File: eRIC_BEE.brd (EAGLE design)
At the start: 25.2 x 34 mm, 40 parts

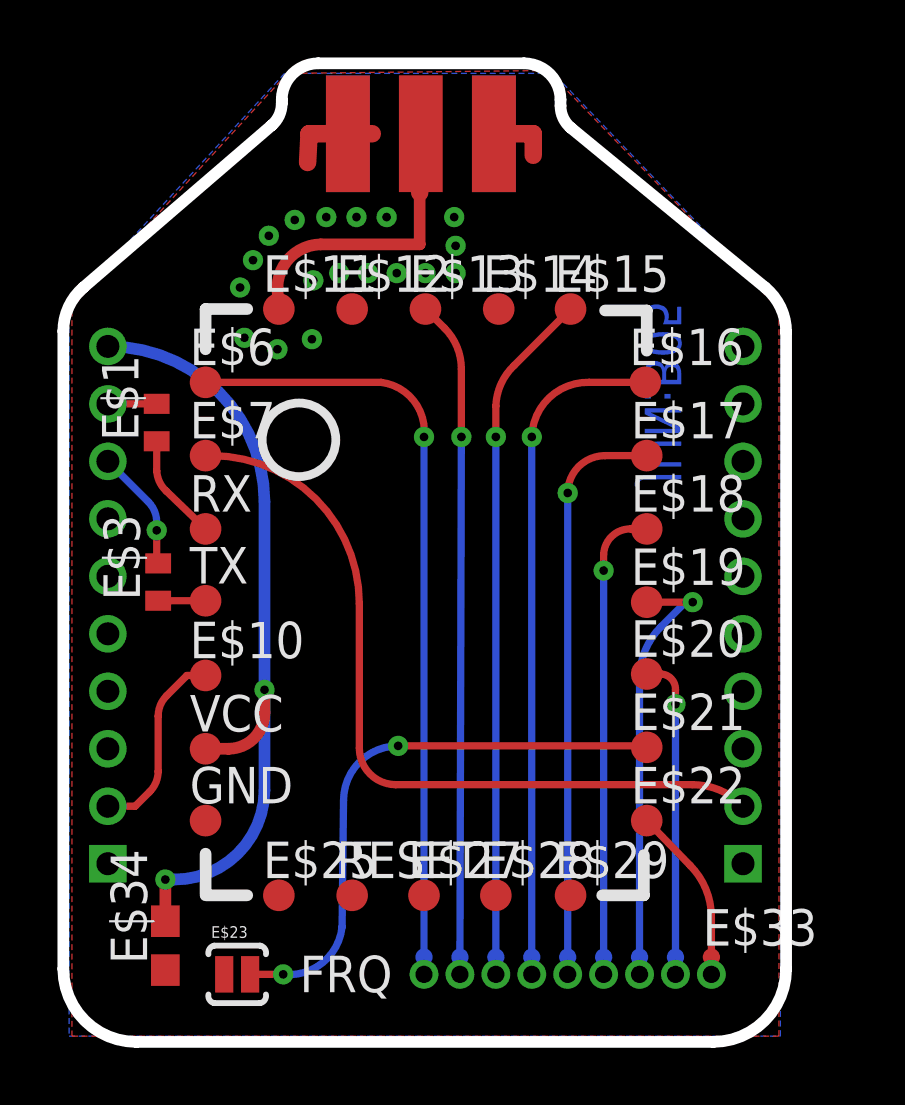
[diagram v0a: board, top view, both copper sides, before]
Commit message: board outline, widen pin spacing, move SMA connector forward
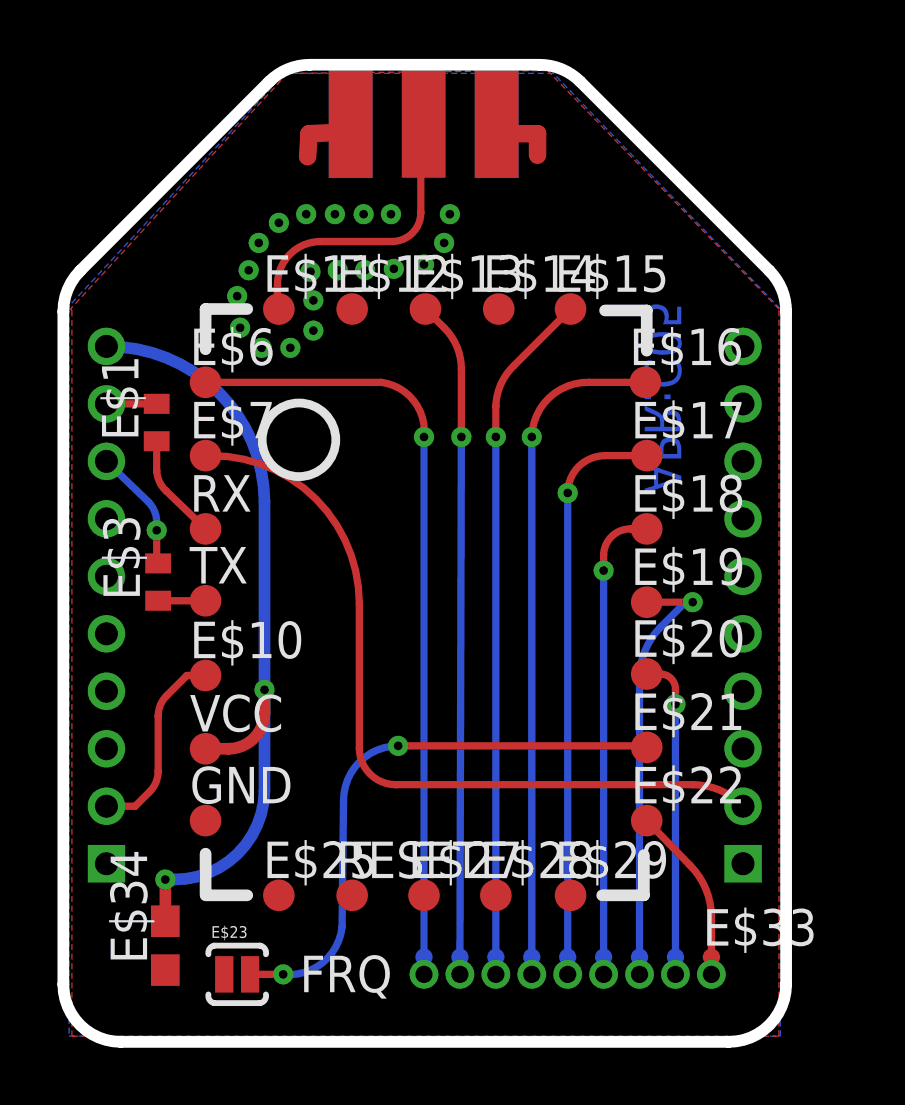
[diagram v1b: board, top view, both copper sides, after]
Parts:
- moved E$44 0.51 mm to (17.9, 47.5)
- moved E$24 0.05 mm to (9.45, 21.6)
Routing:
- net GND: track 5.25 -> 4.10 mm, vias 18 -> 20
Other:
- outline, holes or cut-outs redrawn
- board text added: "APR:C05"
- board text removed: "JUN:B05"
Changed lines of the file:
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@@
 <wire x1="28.25" y1="40.8" x2="26.8" y2="40.8" width="0.4064" layer="121"/>
 <wire x1="28.25" y1="39.4" x2="28.25" y2="40.8" width="0.4064" layer="121"/>
-<wire x1="15.20244375" y1="47.243825" x2="8.6451125" y2="41.598440625" width="0.4064" layer="20"/>
-<wire x1="8.6451125" y1="41.598440625" x2="7.95" y2="40.082765625" width="0.4064" layer="20" curve="49.273877"/>
-<wire x1="7.95" y1="40.082765625" x2="7.95" y2="17.89" width="0.4064" layer="20"/>
-<wire x1="7.95" y1="17.89" x2="10.49" y2="15.35" width="0.4064" layer="20" curve="90"/>
-<wire x1="10.49" y1="15.35" x2="30.56" y2="15.35" width="0.4064" layer="20"/>
-<wire x1="30.56" y1="15.35" x2="33.1" y2="17.89" width="0.4064" layer="20" curve="90"/>
-<wire x1="33.1" y1="17.89" x2="33.1" y2="40.054784375" width="0.4064" layer="20"/>
-<wire x1="33.1" y1="40.054784375" x2="32.3696875" y2="41.600065625" width="0.4064" layer="20" curve="50.591606"/>
-<wire x1="32.3696875" y1="41.600065625" x2="25.61515625" y2="47.149965625" width="0.4064" layer="20"/>
-<wire x1="25.61515625" y1="47.149965625" x2="25.25" y2="47.92260625" width="0.4064" layer="20" curve="-50.591606"/>
-<wire x1="25.25" y1="47.92260625" x2="25.25" y2="48.13" width="0.4064" layer="20"/>
-<wire x1="25.25" y1="48.13" x2="23.98" y2="49.4" width="0.4064" layer="20" curve="90"/>
-<wire x1="23.98" y1="49.4" x2="16.82" y2="49.4" width="0.4064" layer="20"/>
-<wire x1="16.82" y1="49.4" x2="15.55" y2="48.13" width="0.4064" layer="20" curve="90"/>
-<wire x1="15.55" y1="48.13" x2="15.55" y2="48.0016625" width="0.4064" layer="20"/>
-<wire x1="15.55" y1="48.0016625" x2="15.20244375" y2="47.243825" width="0.4064" layer="20" curve="-49.273908"/>
+<wire x1="9.95" y1="15.35" x2="31.1" y2="15.35" width="0.4064" layer="20"/>
+<wire x1="31.1" y1="15.35" x2="33.1" y2="17.35" width="0.4064" layer="20" curve="90"/>
+<wire x1="33.1" y1="17.35" x2="33.1" y2="40.77156875" width="0.4064" layer="20"/>
+<wire x1="33.1" y1="40.77156875" x2="32.5142125" y2="42.185784375" width="0.4064" layer="20" curve="45.000063"/>
+<wire x1="32.5142125" y1="42.185784375" x2="25.9357875" y2="48.7642125" width="0.4064" layer="20"/>
+<wire x1="25.9357875" y1="48.7642125" x2="24.521571875" y2="49.35" width="0.4064" layer="20" curve="45.00009"/>
+<wire x1="24.521571875" y1="49.35" x2="16.528953125" y2="49.35" width="0.4064" layer="20"/>
+<wire x1="16.528953125" y1="49.35" x2="15.11410625" y2="48.76358125" width="0.4064" layer="20" curve="45.025638"/>
+<wire x1="15.11410625" y1="48.76358125" x2="8.535153125" y2="42.178725" width="0.4064" layer="20"/>
+<wire x1="8.535153125" y1="42.178725" x2="7.95" y2="40.76514375" width="0.4064" layer="20" curve="44.974388"/>
+<wire x1="7.95" y1="40.76514375" x2="7.95" y2="17.35" width="0.4064" layer="20"/>
+<wire x1="7.95" y1="17.35" x2="9.95" y2="15.35" width="0.4064" layer="20" curve="90"/>
 <text x="19.4" y="18.35" size="1.27" layer="121" font="vector" ratio="16" rot="R180">FRQ</text>
-<text x="29.45" y="41.15" size="1.27" layer="16" font="vector" ratio="16" rot="MR270">JUN:B05</text>
+<text x="29.45" y="41.15" size="1.27" layer="16" font="vector" ratio="16" rot="MR270">APR:C05</text>
 </plain>
 <attributes>
@@
 <element name="E$28" library="testpad" package="TP11R" value="" x="23" y="20.45"/>
 <element name="E$29" library="testpad" package="TP11R" value="" x="25.6" y="20.45"/>
-<element name="E$44" library="SparkFun-Connectors" package="SMA-EDGE" value="" x="17.85" y="46.95"/>
+<element name="E$44" library="SparkFun-Connectors" package="SMA-EDGE" value="" x="17.95" y="47.45"/>
 <element name="E$23" library="SparkFun-Capacitors" package="SJ_2S-NO" value="" x="14" y="17.7"/>
-<element name="E$24" library="SparkFun-Connectors" package="1X10-2MM" value="" x="9.5" y="21.55" rot="MR90"/>
+<element name="E$24" library="SparkFun-Connectors" package="1X10-2MM" value="" x="9.45" y="21.55" rot="MR90"/>
 <element name="E$26" library="SparkFun-Connectors" package="1X10-2MM" value="" x="31.6" y="21.55" rot="MR90"/>
 <element name="E$2" library="testpad" package="TP06R" value="" x="20.5" y="18.3" rot="MR0"/>
@@
 <contactref element="E$44" pad="GND@1"/>
 <contactref element="E$44" pad="GND@3"/>
-<wire x1="18.7" y1="46.95" x2="16.5" y2="46.95" width="0.6096" layer="1"/>
-<wire x1="16.5" y1="46.95" x2="16.45" y2="45.95" width="0.6096" layer="1"/>
-<wire x1="23" y1="46.95" x2="24.3" y2="46.95" width="0.6096" layer="1"/>
-<wire x1="24.3" y1="46.95" x2="24.3" y2="46.2" width="0.6096" layer="1"/>
+<wire x1="17.6" y1="47" x2="16.5" y2="46.95" width="0.6096" layer="1"/>
+<wire x1="16.5" y1="46.95" x2="16.45" y2="46.15" width="0.6096" layer="1"/>
+<wire x1="23" y1="46.95" x2="24.45" y2="46.95" width="0.6096" layer="1"/>
+<wire x1="24.45" y1="46.95" x2="24.45" y2="46.2" width="0.6096" layer="1"/>
 <contactref element="E$34" pad="1"/>
-<via x="14.1" y="41.6" extent="1-16" drill="0.3"/>
-<via x="14.55" y="42.55" extent="1-16" drill="0.3"/>
-<via x="15.1" y="43.4" extent="1-16" drill="0.3"/>
-<via x="16" y="43.95" extent="1-16" drill="0.3"/>
-<via x="17.1" y="44.05" extent="1-16" drill="0.3"/>
-<via x="18.15" y="44.05" extent="1-16" drill="0.3"/>
-<via x="19.2" y="44.05" extent="1-16" drill="0.3"/>
-<via x="21.55" y="44.05" extent="1-16" drill="0.3"/>
-<via x="21.6" y="43.05" extent="1-16" drill="0.3"/>
-<via x="21.6" y="42.1" extent="1-16" drill="0.3"/>
-<via x="20.55" y="42.1" extent="1-16" drill="0.3"/>
-<via x="19.55" y="42.1" extent="1-16" drill="0.3"/>
-<via x="18.55" y="42.1" extent="1-16" drill="0.3"/>
-<via x="17.55" y="42.1" extent="1-16" drill="0.3"/>
-<via x="16.65" y="41.85" extent="1-16" drill="0.3"/>
-<via x="14.25" y="39.85" extent="1-16" drill="0.3"/>
-<via x="16.6" y="39.8" extent="1-16" drill="0.3"/>
-<via x="15.4" y="39.45" extent="1-16" drill="0.3"/>
+<via x="14.4" y="42.2" extent="1-16" drill="0.3"/>
+<via x="14.75" y="43.15" extent="1-16" drill="0.3"/>
+<via x="15.45" y="43.85" extent="1-16" drill="0.3"/>
+<via x="16.4" y="44.15" extent="1-16" drill="0.3"/>
+<via x="17.4" y="44.15" extent="1-16" drill="0.3"/>
+<via x="18.4" y="44.15" extent="1-16" drill="0.3"/>
+<via x="19.35" y="44.15" extent="1-16" drill="0.3"/>
+<via x="21.4" y="44.15" extent="1-16" drill="0.3"/>
+<via x="21.2" y="43.15" extent="1-16" drill="0.3"/>
+<via x="14" y="41.3" extent="1-16" drill="0.3"/>
+<via x="20.5" y="42.4" extent="1-16" drill="0.3"/>
+<via x="19.45" y="42.25" extent="1-16" drill="0.3"/>
+<via x="18.45" y="42.2" extent="1-16" drill="0.3"/>
+<via x="17.5" y="42.2" extent="1-16" drill="0.3"/>
+<via x="16.55" y="42.15" extent="1-16" drill="0.3"/>
+<via x="14.85" y="39.5" extent="1-16" drill="0.3"/>
+<via x="16.65" y="40.1" extent="1-16" drill="0.3"/>
+<via x="15.85" y="39.5" extent="1-16" drill="0.3"/>
+<via x="14.1" y="40.2" extent="1-16" drill="0.3"/>
+<via x="16.65" y="41.15" extent="1-16" drill="0.3"/>
 </signal>
 <signal name="ANT">
 <contactref element="E$11" pad="TP"/>
 <contactref element="E$44" pad="SIG"/>
-<wire x1="20.39" y1="46.95" x2="20.39" y2="46.21" width="0.6096" layer="1"/>
-<wire x1="20.39" y1="46.21" x2="20.35" y2="44.9" width="0.6096" layer="1"/>
-<wire x1="20.35" y1="44.9" x2="20.35" y2="43.1" width="0.4064" layer="1"/>
-<wire x1="20.35" y1="43.1" x2="16.9" y2="43.1" width="0.4064" layer="1"/>
-<wire x1="16.9" y1="43.1" x2="15.4" y2="41.6" width="0.4064" layer="1" curve="88.05794"/>
-<wire x1="15.4" y1="41.6" x2="15.45" y2="40.85" width="0.4064" layer="1" curve="3.883882"/>
+<wire x1="20.49" y1="47.45" x2="20.39" y2="46.21" width="0.6096" layer="1"/>
+<wire x1="20.39" y1="46.21" x2="20.39" y2="44.2" width="0.254" layer="1"/>
+<wire x1="20.39" y1="44.2" x2="19.39" y2="43.2" width="0.254" layer="1" curve="-90"/>
+<wire x1="19.39" y1="43.2" x2="16.9" y2="43.2" width="0.254" layer="1"/>
+<wire x1="16.9" y1="43.2" x2="15.4" y2="41.7" width="0.254" layer="1" curve="90"/>
+<wire x1="15.4" y1="41.7" x2="15.4" y2="40.9" width="0.254" layer="1"/>
+<wire x1="15.4" y1="40.9" x2="15.45" y2="40.85" width="0.254" layer="1" curve="90"/>
 </signal>
 <signal name="S$27">
@@
 <wire x1="11.2" y1="33.15" x2="11.2" y2="33.4357875" width="0.254" layer="16"/>
 <wire x1="11.2" y1="33.4357875" x2="10.90710625" y2="34.14289375" width="0.254" layer="16" curve="45"/>
-<wire x1="10.90710625" y1="34.14289375" x2="9.5" y2="35.55" width="0.254" layer="16"/>
+<wire x1="10.90710625" y1="34.14289375" x2="9.45" y2="35.55" width="0.254" layer="16"/>
 </signal>
 <signal name="S$14">
@@
 <contactref element="E$1" pad="2"/>
 <contactref element="E$24" pad="9"/>
-<wire x1="9.5" y1="37.55" x2="11.2" y2="37.55" width="0.254" layer="1"/>
+<wire x1="9.45" y1="37.55" x2="11.2" y2="37.55" width="0.254" layer="1"/>
 </signal>
 <signal name="S$3">
@@
 <wire x1="11.25" y1="24.7642125" x2="10.95710625" y2="24.05710625" width="0.254" layer="1" curve="-45"/>
 <wire x1="10.95710625" y1="24.05710625" x2="10.45" y2="23.55" width="0.254" layer="1"/>
-<wire x1="10.45" y1="23.55" x2="9.5" y2="23.55" width="0.254" layer="1"/>
+<wire x1="10.45" y1="23.55" x2="9.45" y2="23.55" width="0.254" layer="1"/>
 </signal>
 <signal name="S$7">
 <contactref element="VCC" pad="TP"/>
 <contactref element="E$24" pad="10"/>
-<wire x1="9.5" y1="39.55" x2="14.95" y2="34.15" width="0.4064" layer="16" curve="-90"/>
+<wire x1="9.45" y1="39.55" x2="14.95" y2="34.15" width="0.4064" layer="16" curve="-90"/>
 <wire x1="14.95" y1="34.15" x2="14.95" y2="27.6" width="0.4064" layer="16"/>
 <via x="14.95" y="27.6" extent="1-16" drill="0.3"/>

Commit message: BOM, component names and values
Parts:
- C1: value (none) -> .1uF
- R1, R2: value (none) -> 10K
- renumbered E$1 to R1, E$23 to J1, E$24 to H1, E$26 to H2, E$3 to R2, E$34 to C1, E$44 to SMA
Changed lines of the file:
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@@
 <element name="E$28" library="testpad" package="TP11R" value="" x="23" y="20.45"/>
 <element name="E$29" library="testpad" package="TP11R" value="" x="25.6" y="20.45"/>
-<element name="E$44" library="SparkFun-Connectors" package="SMA-EDGE" value="" x="17.95" y="47.45"/>
-<element name="E$23" library="SparkFun-Capacitors" package="SJ_2S-NO" value="" x="14" y="17.7"/>
-<element name="E$24" library="SparkFun-Connectors" package="1X10-2MM" value="" x="9.45" y="21.55" rot="MR90"/>
-<element name="E$26" library="SparkFun-Connectors" package="1X10-2MM" value="" x="31.6" y="21.55" rot="MR90"/>
+<element name="SMA" library="SparkFun-Connectors" package="SMA-EDGE" value="" x="17.95" y="47.45"/>
+<element name="J1" library="SparkFun-Capacitors" package="SJ_2S-NO" value="" x="14" y="17.7"/>
+<element name="H1" library="SparkFun-Connectors" package="1X10-2MM" value="" x="9.45" y="21.55" rot="MR90"/>
+<element name="H2" library="SparkFun-Connectors" package="1X10-2MM" value="" x="31.6" y="21.55" rot="MR90"/>
 <element name="E$2" library="testpad" package="TP06R" value="" x="20.5" y="18.3" rot="MR0"/>
 <element name="E$4" library="testpad" package="TP06R" value="" x="21.75" y="18.3" rot="MR0"/>
@@
 <element name="E$32" library="testpad" package="TP06R" value="" x="29.25" y="18.3" rot="MR0"/>
 <element name="E$33" library="testpad" package="TP06R" value="" x="30.5" y="18.3"/>
-<element name="E$1" library="ref-packages" package="R0402" value="" x="11.2" y="36.9" rot="R90"/>
-<element name="E$3" library="ref-packages" package="R0402" value="" x="11.25" y="31.35" rot="R90"/>
-<element name="E$34" library="eagle-ltspice" package="C0603" value="" x="11.5" y="18.7" rot="R90"/>
+<element name="R1" library="ref-packages" package="R0402" value="10K" x="11.2" y="36.9" rot="R90"/>
+<element name="R2" library="ref-packages" package="R0402" value="10K" x="11.25" y="31.35" rot="R90"/>
+<element name="C1" library="eagle-ltspice" package="C0603" value=".1uF" x="11.5" y="18.7" rot="R90"/>
 </elements>
 <signals>
 <signal name="GND">
 <polygon width="0.4064" layer="1">
-<vertex x="8.25" y="40.8"/>
-<vertex x="8.25" y="15.55"/>
-<vertex x="32.85" y="15.55"/>
-<vertex x="32.85" y="40.85"/>
+<vertex x="15.75" y="49.05"/>
+<vertex x="8.538225" y="41.74206875" curve="44.620557"/>
+<vertex x="8.25" y="41.039659375"/>
+<vertex x="8.25" y="16.55" curve="90"/>
+<vertex x="9.25" y="15.55"/>
+<vertex x="31.85" y="15.55" curve="90"/>
+<vertex x="32.85" y="16.55"/>
+<vertex x="32.80084375" y="40.8331875" curve="45.248454"/>
+<vertex x="32.503490625" y="41.542803125"/>
 <vertex x="24.8" y="49.15"/>
-<vertex x="15.75" y="49.05"/>
-<vertex x="8.2" y="40.85"/>
 </polygon>
 <polygon width="0.254" layer="16">
-<vertex x="8.15" y="40.9"/>
-<vertex x="8.15" y="15.55"/>
-<vertex x="32.9" y="15.55"/>
-<vertex x="32.9" y="40.85"/>
+<vertex x="8.15" y="41.4"/>
+<vertex x="8.15" y="16.55" curve="90"/>
+<vertex x="9.15" y="15.55"/>
+<vertex x="31.9" y="15.55" curve="90"/>
+<vertex x="32.9" y="16.55"/>
+<vertex x="32.85" y="41.3"/>
 <vertex x="25" y="49.05"/>
 <vertex x="15.65" y="49.05"/>
-<vertex x="8.1" y="40.9"/>
 </polygon>
-<contactref element="E$24" pad="1"/>
+<contactref element="H1" pad="1"/>
 <contactref element="GND" pad="TP"/>
-<contactref element="E$23" pad="1"/>
+<contactref element="J1" pad="1"/>
 <contactref element="E$12" pad="TP"/>
-<contactref element="E$44" pad="GND@0"/>
-<contactref element="E$44" pad="GND@2"/>
-<contactref element="E$44" pad="GND@1"/>
-<contactref element="E$44" pad="GND@3"/>
+<contactref element="SMA" pad="GND@0"/>
+<contactref element="SMA" pad="GND@2"/>
+<contactref element="SMA" pad="GND@1"/>
+<contactref element="SMA" pad="GND@3"/>
 <wire x1="17.6" y1="47" x2="16.5" y2="46.95" width="0.6096" layer="1"/>
 <wire x1="16.5" y1="46.95" x2="16.45" y2="46.15" width="0.6096" layer="1"/>
 <wire x1="23" y1="46.95" x2="24.45" y2="46.95" width="0.6096" layer="1"/>
 <wire x1="24.45" y1="46.95" x2="24.45" y2="46.2" width="0.6096" layer="1"/>
-<contactref element="E$34" pad="1"/>
+<contactref element="C1" pad="1"/>
 <via x="14.4" y="42.2" extent="1-16" drill="0.3"/>
 <via x="14.75" y="43.15" extent="1-16" drill="0.3"/>
@@
 <signal name="ANT">
 <contactref element="E$11" pad="TP"/>
-<contactref element="E$44" pad="SIG"/>
+<contactref element="SMA" pad="SIG"/>
 <wire x1="20.49" y1="47.45" x2="20.39" y2="46.21" width="0.6096" layer="1"/>
 <wire x1="20.39" y1="46.21" x2="20.39" y2="44.2" width="0.254" layer="1"/>
@@
 </signal>
 <signal name="S$27">
-<contactref element="E$3" pad="2"/>
-<contactref element="E$24" pad="8"/>
+<contactref element="R2" pad="2"/>
+<contactref element="H1" pad="8"/>
 <wire x1="11.25" y1="32" x2="11.2" y2="32.05" width="0.254" layer="1"/>
 <wire x1="11.2" y1="32.05" x2="11.2" y2="33.15" width="0.254" layer="1"/>
@@
 <signal name="S$14">
 <contactref element="TX" pad="TP"/>
-<contactref element="E$3" pad="1"/>
+<contactref element="R2" pad="1"/>
 <wire x1="11.25" y1="30.7" x2="12.9" y2="30.7" width="0.254" layer="1"/>
 </signal>
 <signal name="S$28">
-<contactref element="E$1" pad="2"/>
-<contactref element="E$24" pad="9"/>
+<contactref element="R1" pad="2"/>
+<contactref element="H1" pad="9"/>
 <wire x1="9.45" y1="37.55" x2="11.2" y2="37.55" width="0.254" layer="1"/>
 </signal>
 <signal name="S$3">
 <contactref element="RX" pad="TP"/>
-<contactref element="E$1" pad="1"/>
+<contactref element="R1" pad="1"/>
 <wire x1="12.9" y1="33.2" x2="11.54289375" y2="34.50710625" width="0.254" layer="1"/>
 <wire x1="11.54289375" y1="34.50710625" x2="11.2" y2="35.2142125" width="0.254" layer="1" curve="-45"/>
@@
 <signal name="S$6">
 <contactref element="E$10" pad="TP"/>
-<contactref element="E$24" pad="2"/>
+<contactref element="H1" pad="2"/>
 <wire x1="12.9" y1="28.1" x2="12.25" y2="28.1" width="0.254" layer="1"/>
 <wire x1="12.25" y1="28.1" x2="11.54289375" y2="27.39289375" width="0.254" layer="1"/>
@@
 <signal name="S$7">
 <contactref element="VCC" pad="TP"/>
-<contactref element="E$24" pad="10"/>
+<contactref element="H1" pad="10"/>
 <wire x1="9.45" y1="39.55" x2="14.95" y2="34.15" width="0.4064" layer="16" curve="-90"/>
 <wire x1="14.95" y1="34.15" x2="14.95" y2="27.6" width="0.4064" layer="16"/>
 <via x="14.95" y="27.6" extent="1-16" drill="0.3"/>
-<contactref element="E$34" pad="2"/>
+<contactref element="C1" pad="2"/>
 <wire x1="11.5" y1="19.55" x2="11.5" y2="21" width="0.4064" layer="1"/>
 <via x="11.5" y="21" extent="1-16" drill="0.3"/>
@@
 <signal name="S$8">
 <contactref element="E$7" pad="TP"/>
-<contactref element="E$26" pad="2"/>
+<contactref element="H2" pad="2"/>
 <wire x1="29.847896875" y1="24.3" x2="19.52" y2="24.3" width="0.254" layer="1"/>
 <wire x1="19.52" y1="24.3" x2="18.25" y2="25.57" width="0.254" layer="1" curve="-90"/>
@@
 </signal>
 <signal name="S$1">
-<contactref element="E$23" pad="2"/>
+<contactref element="J1" pad="2"/>
 <contactref element="E$21" pad="TP"/>
 <wire x1="28.25" y1="25.6" x2="28.129290625" y2="25.65" width="0.254" layer="1" curve="45"/>
